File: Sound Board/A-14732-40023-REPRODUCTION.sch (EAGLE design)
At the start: 220 parts, among them P6 POWER, P7 SPEAKER, Q1 MPS3646, U1 OKI6295, U10 26LS32A, U11 26LS31, U12 27C040-150, U13 27C040-150, U14 YAMAHA 2151, U15 TIL7524, U16 74LS374, U17 74LS174, U18 16L8, U19 74LS11, U2 2064, U20 74LS139, U21 74LS14, U22 74LS74, U23 74LS74, U24 26LS31, U25 26LS32A, U26 74LS04, U28 YAMAHA 3012, U29 LM324D, U3 27C040, U30 MC3340, U31 MB3731, U32 TL084D, U33 TL084D, U4 6809E, U5 74LS374DW, U6 26LS32A, U7 26LS31, U8 74LS138, U9 74LS74, Y1 3.5749MHz, Y2 8MHz

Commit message: fixes
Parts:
- VR1: device MK-ICs:7809D2PAK -> MK-ICs:7809TO220
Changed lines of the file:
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@@
 <grid distance="0.1" unitdist="inch" unit="inch" style="lines" multiple="1" display="yes" altdistance="0.01" altunitdist="inch" altunit="inch"/>
 <layers>
-<layer number="1" name="Top" color="4" fill="1" visible="no" active="no"/>
-<layer number="2" name="Route2" color="1" fill="3" visible="no" active="no"/>
-<layer number="3" name="Route3" color="4" fill="3" visible="no" active="no"/>
-<layer number="4" name="Route4" color="1" fill="4" visible="no" active="no"/>
-<layer number="5" name="Route5" color="4" fill="4" visible="no" active="no"/>
-<layer number="6" name="Route6" color="1" fill="8" visible="no" active="no"/>
-<layer number="7" name="Route7" color="4" fill="8" visible="no" active="no"/>
-<layer number="8" name="Route8" color="1" fill="2" visible="no" active="no"/>
-<layer number="9" name="Route9" color="4" fill="2" visible="no" active="no"/>
-<layer number="10" name="Route10" color="1" fill="7" visible="no" active="no"/>
-<layer number="11" name="Route11" color="4" fill="7" visible="no" active="no"/>
-<layer number="12" name="Route12" color="1" fill="5" visible="no" active="no"/>
-<layer number="13" name="Route13" color="4" fill="5" visible="no" active="no"/>
-<layer number="14" name="Route14" color="1" fill="6" visible="no" active="no"/>
-<layer number="15" name="Route15" color="4" fill="6" visible="no" active="no"/>
-<layer number="16" name="Bottom" color="1" fill="1" visible="no" active="no"/>
-<layer number="17" name="Pads" color="2" fill="1" visible="no" active="no"/>
-<layer number="18" name="Vias" color="2" fill="1" visible="no" active="no"/>
-<layer number="19" name="Unrouted" color="6" fill="1" visible="no" active="no"/>
-<layer number="20" name="Dimension" color="15" fill="1" visible="no" active="no"/>
-<layer number="21" name="tPlace" color="7" fill="1" visible="no" active="no"/>
-<layer number="22" name="bPlace" color="7" fill="1" visible="no" active="no"/>
-<layer number="23" name="tOrigins" color="15" fill="1" visible="no" active="no"/>
-<layer number="24" name="bOrigins" color="15" fill="1" visible="no" active="no"/>
-<layer number="25" name="tNames" color="7" fill="1" visible="no" active="no"/>
-<layer number="26" name="bNames" color="7" fill="1" visible="no" active="no"/>
-<layer number="27" name="tValues" color="7" fill="1" visible="no" active="no"/>
-<layer number="28" name="bValues" color="7" fill="1" visible="no" active="no"/>
+<layer number="1" name="Top" color="4" fill="1" visible="yes" active="no"/>
+<layer number="2" name="Route2" color="1" fill="3" visible="yes" active="no"/>
+<layer number="3" name="Route3" color="4" fill="3" visible="yes" active="no"/>
+<layer number="4" name="Route4" color="1" fill="4" visible="yes" active="no"/>
+<layer number="5" name="Route5" color="4" fill="4" visible="yes" active="no"/>
+<layer number="6" name="Route6" color="1" fill="8" visible="yes" active="no"/>
+<layer number="7" name="Route7" color="4" fill="8" visible="yes" active="no"/>
+<layer number="8" name="Route8" color="1" fill="2" visible="yes" active="no"/>
+<layer number="9" name="Route9" color="4" fill="2" visible="yes" active="no"/>
+<layer number="10" name="Route10" color="1" fill="7" visible="yes" active="no"/>
+<layer number="11" name="Route11" color="4" fill="7" visible="yes" active="no"/>
+<layer number="12" name="Route12" color="1" fill="5" visible="yes" active="no"/>
+<layer number="13" name="Route13" color="4" fill="5" visible="yes" active="no"/>
+<layer number="14" name="Route14" color="1" fill="6" visible="yes" active="no"/>
+<layer number="15" name="Route15" color="4" fill="6" visible="yes" active="no"/>
+<layer number="16" name="Bottom" color="1" fill="1" visible="yes" active="no"/>
+<layer number="17" name="Pads" color="2" fill="1" visible="yes" active="no"/>
+<layer number="18" name="Vias" color="2" fill="1" visible="yes" active="no"/>
+<layer number="19" name="Unrouted" color="6" fill="1" visible="yes" active="no"/>
+<layer number="20" name="Dimension" color="15" fill="1" visible="yes" active="no"/>
+<layer number="21" name="tPlace" color="7" fill="1" visible="yes" active="no"/>
+<layer number="22" name="bPlace" color="7" fill="1" visible="yes" active="no"/>
+<layer number="23" name="tOrigins" color="15" fill="1" visible="yes" active="no"/>
+<layer number="24" name="bOrigins" color="15" fill="1" visible="yes" active="no"/>
+<layer number="25" name="tNames" color="7" fill="1" visible="yes" active="no"/>
+<layer number="26" name="bNames" color="7" fill="1" visible="yes" active="no"/>
+<layer number="27" name="tValues" color="7" fill="1" visible="yes" active="no"/>
+<layer number="28" name="bValues" color="7" fill="1" visible="yes" active="no"/>
 <layer number="29" name="tStop" color="7" fill="3" visible="no" active="no"/>
 <layer number="30" name="bStop" color="7" fill="6" visible="no" active="no"/>
@@
 <layer number="35" name="tGlue" color="7" fill="4" visible="no" active="no"/>
 <layer number="36" name="bGlue" color="7" fill="5" visible="no" active="no"/>
-<layer number="37" name="tTest" color="7" fill="1" visible="no" active="no"/>
-<layer number="38" name="bTest" color="7" fill="1" visible="no" active="no"/>
+<layer number="37" name="tTest" color="7" fill="1" visible="yes" active="no"/>
+<layer number="38" name="bTest" color="7" fill="1" visible="yes" active="no"/>
 <layer number="39" name="tKeepout" color="4" fill="11" visible="no" active="no"/>
 <layer number="40" name="bKeepout" color="1" fill="11" visible="no" active="no"/>
@@
 <layer number="44" name="Drills" color="7" fill="1" visible="no" active="no"/>
 <layer number="45" name="Holes" color="7" fill="1" visible="no" active="no"/>
-<layer number="46" name="Milling" color="3" fill="1" visible="no" active="no"/>
-<layer number="47" name="Measures" color="7" fill="1" visible="no" active="no"/>
-<layer number="48" name="Document" color="7" fill="1" visible="no" active="no"/>
-<layer number="49" name="Reference" color="7" fill="1" visible="no" active="no"/>
-<layer number="50" name="dxf" color="7" fill="1" visible="no" active="no"/>
-<layer number="51" name="tDocu" color="7" fill="1" visible="no" active="no"/>
-<layer number="52" name="bDocu" color="7" fill="1" visible="no" active="no"/>
-<layer number="53" name="tGND_GNDA" color="7" fill="9" visible="no" active="no"/>
-<layer number="54" name="bGND_GNDA" color="1" fill="9" visible="no" active="no"/>
-<layer number="56" name="wert" color="7" fill="1" visible="no" active="no"/>
-<layer number="57" name="tCAD" color="7" fill="1" visible="no" active="no"/>
-<layer number="59" name="tCarbon" color="7" fill="1" visible="no" active="no"/>
-<layer number="60" name="bCarbon" color="7" fill="1" visible="no" active="no"/>
+<layer number="46" name="Milling" color="3" fill="1" visible="yes" active="no"/>
+<layer number="47" name="Measures" color="7" fill="1" visible="yes" active="no"/>
+<layer number="48" name="Document" color="7" fill="1" visible="yes" active="no"/>
+<layer number="49" name="Reference" color="7" fill="1" visible="yes" active="no"/>
+<layer number="50" name="dxf" color="7" fill="1" visible="yes" active="no"/>
+<layer number="51" name="tDocu" color="7" fill="1" visible="yes" active="no"/>
+<layer number="52" name="bDocu" color="7" fill="1" visible="yes" active="no"/>
+<layer number="53" name="tGND_GNDA" color="7" fill="9" visible="yes" active="no"/>
+<layer number="54" name="bGND_GNDA" color="1" fill="9" visible="yes" active="no"/>
+<layer number="56" name="wert" color="7" fill="1" visible="yes" active="no"/>
+<layer number="57" name="tCAD" color="7" fill="1" visible="yes" active="no"/>
+<layer number="59" name="tCarbon" color="7" fill="1" visible="yes" active="no"/>
+<layer number="60" name="bCarbon" color="7" fill="1" visible="yes" active="no"/>
 <layer number="90" name="Modules" color="5" fill="1" visible="yes" active="yes"/>
 <layer number="91" name="Nets" color="2" fill="1" visible="yes" active="yes"/>
@@
 <part name="R87" library="SparkFun-Passives" deviceset="RESISTOR" device="0805-RES" value="3.9K"/>
 <part name="U$35" library="SparkFun-Aesthetics" deviceset="AGND" device=""/>
-<part name="VR1" library="MK-ICs" deviceset="7809" device="D2PAK" value="7809">
+<part name="VR1" library="MK-ICs" deviceset="7809" device="TO220" value="7809">
 <attribute name="PARTNUMBER" value="5460-12743-00"/>
 </part>

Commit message: corrected library for SRAM and ROM chips
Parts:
- U2: device MK-ICs:MS6264L -> A-14732-40023:MS6264LSOP28
- U3: device MK-ICs:27C040 -> A-14732-40023:27C040
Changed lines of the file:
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@@
 <grid distance="0.1" unitdist="inch" unit="inch" style="lines" multiple="1" display="yes" altdistance="0.01" altunitdist="inch" altunit="inch"/>
 <layers>
-<layer number="1" name="Top" color="4" fill="1" visible="yes" active="no"/>
-<layer number="2" name="Route2" color="1" fill="3" visible="yes" active="no"/>
-<layer number="3" name="Route3" color="4" fill="3" visible="yes" active="no"/>
-<layer number="4" name="Route4" color="1" fill="4" visible="yes" active="no"/>
-<layer number="5" name="Route5" color="4" fill="4" visible="yes" active="no"/>
-<layer number="6" name="Route6" color="1" fill="8" visible="yes" active="no"/>
-<layer number="7" name="Route7" color="4" fill="8" visible="yes" active="no"/>
-<layer number="8" name="Route8" color="1" fill="2" visible="yes" active="no"/>
-<layer number="9" name="Route9" color="4" fill="2" visible="yes" active="no"/>
-<layer number="10" name="Route10" color="1" fill="7" visible="yes" active="no"/>
-<layer number="11" name="Route11" color="4" fill="7" visible="yes" active="no"/>
-<layer number="12" name="Route12" color="1" fill="5" visible="yes" active="no"/>
-<layer number="13" name="Route13" color="4" fill="5" visible="yes" active="no"/>
-<layer number="14" name="Route14" color="1" fill="6" visible="yes" active="no"/>
-<layer number="15" name="Route15" color="4" fill="6" visible="yes" active="no"/>
-<layer number="16" name="Bottom" color="1" fill="1" visible="yes" active="no"/>
-<layer number="17" name="Pads" color="2" fill="1" visible="yes" active="no"/>
-<layer number="18" name="Vias" color="2" fill="1" visible="yes" active="no"/>
-<layer number="19" name="Unrouted" color="6" fill="1" visible="yes" active="no"/>
-<layer number="20" name="Dimension" color="15" fill="1" visible="yes" active="no"/>
-<layer number="21" name="tPlace" color="7" fill="1" visible="yes" active="no"/>
-<layer number="22" name="bPlace" color="7" fill="1" visible="yes" active="no"/>
-<layer number="23" name="tOrigins" color="15" fill="1" visible="yes" active="no"/>
-<layer number="24" name="bOrigins" color="15" fill="1" visible="yes" active="no"/>
-<layer number="25" name="tNames" color="7" fill="1" visible="yes" active="no"/>
-<layer number="26" name="bNames" color="7" fill="1" visible="yes" active="no"/>
-<layer number="27" name="tValues" color="7" fill="1" visible="yes" active="no"/>
-<layer number="28" name="bValues" color="7" fill="1" visible="yes" active="no"/>
+<layer number="1" name="Top" color="4" fill="1" visible="no" active="no"/>
+<layer number="2" name="Route2" color="1" fill="3" visible="no" active="no"/>
+<layer number="3" name="Route3" color="4" fill="3" visible="no" active="no"/>
+<layer number="4" name="Route4" color="1" fill="4" visible="no" active="no"/>
+<layer number="5" name="Route5" color="4" fill="4" visible="no" active="no"/>
+<layer number="6" name="Route6" color="1" fill="8" visible="no" active="no"/>
+<layer number="7" name="Route7" color="4" fill="8" visible="no" active="no"/>
+<layer number="8" name="Route8" color="1" fill="2" visible="no" active="no"/>
+<layer number="9" name="Route9" color="4" fill="2" visible="no" active="no"/>
+<layer number="10" name="Route10" color="1" fill="7" visible="no" active="no"/>
+<layer number="11" name="Route11" color="4" fill="7" visible="no" active="no"/>
+<layer number="12" name="Route12" color="1" fill="5" visible="no" active="no"/>
+<layer number="13" name="Route13" color="4" fill="5" visible="no" active="no"/>
+<layer number="14" name="Route14" color="1" fill="6" visible="no" active="no"/>
+<layer number="15" name="Route15" color="4" fill="6" visible="no" active="no"/>
+<layer number="16" name="Bottom" color="1" fill="1" visible="no" active="no"/>
+<layer number="17" name="Pads" color="2" fill="1" visible="no" active="no"/>
+<layer number="18" name="Vias" color="2" fill="1" visible="no" active="no"/>
+<layer number="19" name="Unrouted" color="6" fill="1" visible="no" active="no"/>
+<layer number="20" name="Dimension" color="15" fill="1" visible="no" active="no"/>
+<layer number="21" name="tPlace" color="7" fill="1" visible="no" active="no"/>
+<layer number="22" name="bPlace" color="7" fill="1" visible="no" active="no"/>
+<layer number="23" name="tOrigins" color="15" fill="1" visible="no" active="no"/>
+<layer number="24" name="bOrigins" color="15" fill="1" visible="no" active="no"/>
+<layer number="25" name="tNames" color="7" fill="1" visible="no" active="no"/>
+<layer number="26" name="bNames" color="7" fill="1" visible="no" active="no"/>
+<layer number="27" name="tValues" color="7" fill="1" visible="no" active="no"/>
+<layer number="28" name="bValues" color="7" fill="1" visible="no" active="no"/>
 <layer number="29" name="tStop" color="7" fill="3" visible="no" active="no"/>
 <layer number="30" name="bStop" color="7" fill="6" visible="no" active="no"/>
@@
 <layer number="35" name="tGlue" color="7" fill="4" visible="no" active="no"/>
 <layer number="36" name="bGlue" color="7" fill="5" visible="no" active="no"/>
-<layer number="37" name="tTest" color="7" fill="1" visible="yes" active="no"/>
-<layer number="38" name="bTest" color="7" fill="1" visible="yes" active="no"/>
+<layer number="37" name="tTest" color="7" fill="1" visible="no" active="no"/>
+<layer number="38" name="bTest" color="7" fill="1" visible="no" active="no"/>
 <layer number="39" name="tKeepout" color="4" fill="11" visible="no" active="no"/>
 <layer number="40" name="bKeepout" color="1" fill="11" visible="no" active="no"/>
@@
 <layer number="44" name="Drills" color="7" fill="1" visible="no" active="no"/>
 <layer number="45" name="Holes" color="7" fill="1" visible="no" active="no"/>
-<layer number="46" name="Milling" color="3" fill="1" visible="yes" active="no"/>
-<layer number="47" name="Measures" color="7" fill="1" visible="yes" active="no"/>
-<layer number="48" name="Document" color="7" fill="1" visible="yes" active="no"/>
-<layer number="49" name="Reference" color="7" fill="1" visible="yes" active="no"/>
-<layer number="50" name="dxf" color="7" fill="1" visible="yes" active="no"/>
-<layer number="51" name="tDocu" color="7" fill="1" visible="yes" active="no"/>
-<layer number="52" name="bDocu" color="7" fill="1" visible="yes" active="no"/>
-<layer number="53" name="tGND_GNDA" color="7" fill="9" visible="yes" active="no"/>
-<layer number="54" name="bGND_GNDA" color="1" fill="9" visible="yes" active="no"/>
-<layer number="56" name="wert" color="7" fill="1" visible="yes" active="no"/>
-<layer number="57" name="tCAD" color="7" fill="1" visible="yes" active="no"/>
-<layer number="59" name="tCarbon" color="7" fill="1" visible="yes" active="no"/>
-<layer number="60" name="bCarbon" color="7" fill="1" visible="yes" active="no"/>
+<layer number="46" name="Milling" color="3" fill="1" visible="no" active="no"/>
+<layer number="47" name="Measures" color="7" fill="1" visible="no" active="no"/>
+<layer number="48" name="Document" color="7" fill="1" visible="no" active="no"/>
+<layer number="49" name="Reference" color="7" fill="1" visible="no" active="no"/>
+<layer number="50" name="dxf" color="7" fill="1" visible="no" active="no"/>
+<layer number="51" name="tDocu" color="7" fill="1" visible="no" active="no"/>
+<layer number="52" name="bDocu" color="7" fill="1" visible="no" active="no"/>
+<layer number="53" name="tGND_GNDA" color="7" fill="9" visible="no" active="no"/>
+<layer number="54" name="bGND_GNDA" color="1" fill="9" visible="no" active="no"/>
+<layer number="56" name="wert" color="7" fill="1" visible="no" active="no"/>
+<layer number="57" name="tCAD" color="7" fill="1" visible="no" active="no"/>
+<layer number="59" name="tCarbon" color="7" fill="1" visible="no" active="no"/>
+<layer number="60" name="bCarbon" color="7" fill="1" visible="no" active="no"/>
 <layer number="90" name="Modules" color="5" fill="1" visible="yes" active="yes"/>
 <layer number="91" name="Nets" color="2" fill="1" visible="yes" active="yes"/>
@@
 <part name="U26" library="74xx-us" deviceset="74*04" device="D" technology="LS" value="74LS04"/>
 <part name="U16" library="74xx-us" deviceset="74*374" device="DW" technology="LS" value="74LS374"/>
-<part name="U2" library="MK-ICs" deviceset="MS6264L" device="" value="2064"/>
+<part name="U2" library="A-14732-40023" deviceset="MS6264L" device="SOP28" value="2064"/>
 <part name="U18" library="MK-ICs" deviceset="PAL16L8" device="" value="16L8"/>
-<part name="U3" library="MK-ICs" deviceset="27C040" device="" value="27C040"/>
+<part name="U3" library="A-14732-40023" deviceset="27C040" device="" value="27C040"/>
 <part name="GND7" library="supply2" deviceset="GND" device=""/>
 <part name="+5V9" library="SparkFun-Aesthetics" deviceset="5V" device=""/>

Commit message: updated other ICs with current library in use
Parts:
- U1: device MK-ICs:OKI6295 -> A-14732-40023:OKI6295
- U12, U13: device MK-ICs:27C040 -> A-14732-40023:27C040PLCC32-SOCKET
- U14: device MK-ICs:YM2151 -> A-14732-40023:YM2151
- U18: device MK-ICs:PAL16L8 -> A-14732-40023:PAL16L8
- U28: device MK-ICs:YM3012 -> A-14732-40023:YM3012
- U3: device A-14732-40023:27C040 -> A-14732-40023:27C040PLCC32-SOCKET

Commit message: fixes
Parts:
- RV1: device SparkFun-Electromechanical:POTALPS-KIT -> SparkFun-Electromechanical:POT-RV16AF-20
- Y1: device crystal:CRYSTALSM49 -> crystal:CRYSTALHC49U-V
- renumbered C79 to C84
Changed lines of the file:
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@@
 <part name="+5V17" library="SparkFun-Aesthetics" deviceset="5V" device=""/>
 <part name="FRAME2" library="SparkFun-Retired" deviceset="FRAME-A3" device=""/>
-<part name="Y1" library="crystal" deviceset="CRYSTAL" device="SM49" value="3.5749MHz">
+<part name="Y1" library="crystal" deviceset="CRYSTAL" device="HC49U-V" value="3.5749MHz">
 <attribute name="TOLERANCE" value="0.01%"/>
 </part>
@@
 <attribute name="TOLERANCE" value="0.01%"/>
 </part>
-<part name="C79" library="A-14732-40023" deviceset="CAP_POL" device="E" value="220uF">
+<part name="C84" library="A-14732-40023" deviceset="CAP_POL" device="E" value="220uF">
 <attribute name="VOLTAGE" value="16V"/>
 </part>
@@
 <attribute name="VOLTAGE" value="50V"/>
 </part>
-<part name="RV1" library="SparkFun-Electromechanical" deviceset="POT" device="ALPS-KIT" value="50K"/>
+<part name="RV1" library="SparkFun-Electromechanical" deviceset="POT" device="-RV16AF-20" value="50K"/>
 <part name="C73" library="A-14732-40023" deviceset="CAP_POL" device="C" value="10uF">
 <attribute name="VOLTAGE" value="20V"/>
@@
 <attribute name="PITCH" x="60.96" y="45.72" size="1.778" layer="96" rot="MR180"/>
 </instance>
-<instance part="C79" gate="G$1" x="241.3" y="111.76">
+<instance part="C84" gate="G$1" x="241.3" y="111.76">
 <attribute name="VOLTAGE" x="243.84" y="109.22" size="1.778" layer="96"/>
 </instance>
@@
 </segment>
 <segment>
-<pinref part="C79" gate="G$1" pin="-"/>
+<pinref part="C84" gate="G$1" pin="-"/>
 <pinref part="U$37" gate="G$1" pin="AGND"/>
 <wire x1="241.3" y1="106.68" x2="241.3" y2="99.06" width="0.1524" layer="91"/>
@@
 <net name="N$92" class="0">
 <segment>
-<pinref part="C79" gate="G$1" pin="+"/>
+<pinref part="C84" gate="G$1" pin="+"/>
 <wire x1="279.4" y1="121.92" x2="243.84" y2="121.92" width="0.1524" layer="91"/>
 <wire x1="243.84" y1="121.92" x2="243.84" y2="119.38" width="0.1524" layer="91"/>

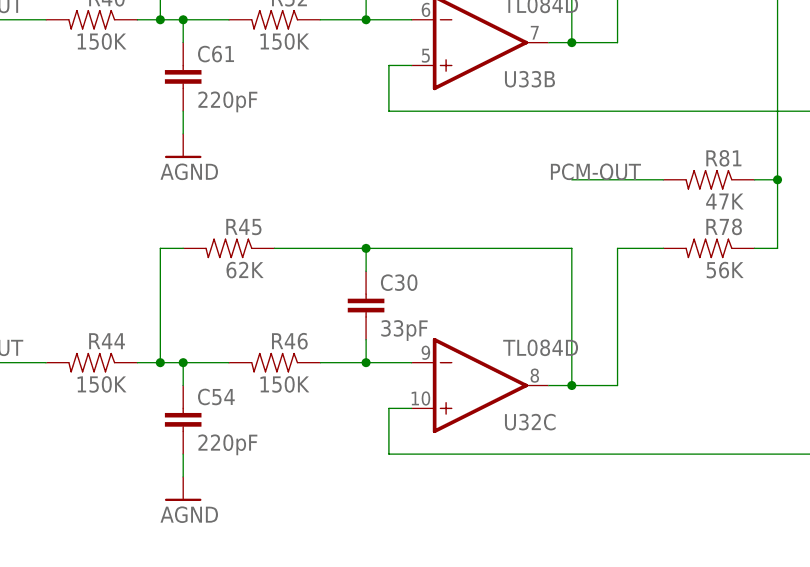
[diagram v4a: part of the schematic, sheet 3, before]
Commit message: corrected C30 to C59
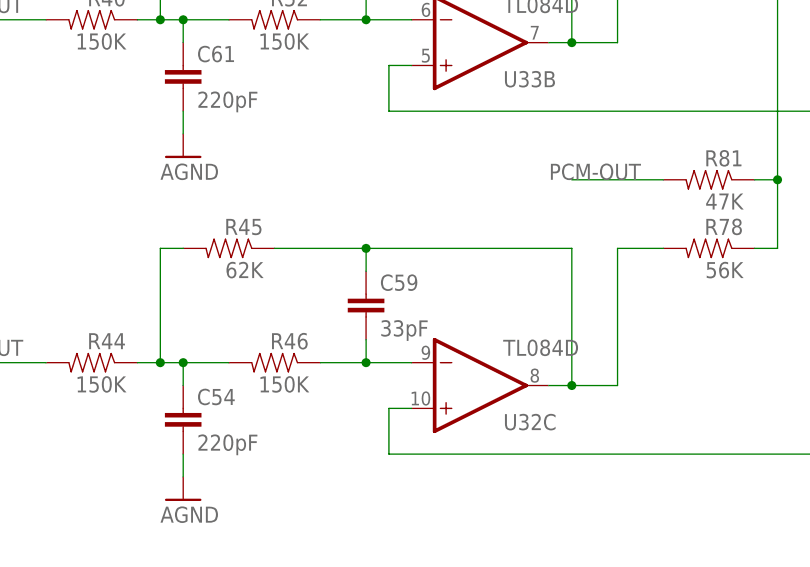
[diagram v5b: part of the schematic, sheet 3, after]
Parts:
- C95: device A-14732-40023:CAP_POLPTH3 -> A-14732-40023:CAP_POLPTH4
- U12, U13, U3: device A-14732-40023:27C040PLCC32-SOCKET -> A-14732-40023:27C040PLCC32
- renumbered C30 to C59
